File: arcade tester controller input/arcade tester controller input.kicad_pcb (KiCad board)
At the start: 2 copper layers, 70.2 x 88 mm, 27 parts, among them J1 FTDI, J2 ICSP, J3 DE9M 1, J4 DE9M 2, J5 Conn_01x08, J6 Conn_01x08, J7 Conn_01x08, J8 Conn_01x08, J9 Conn_01x02, U1 ATmega328P-P, U2 MCP23018, U3 MCP23018, Y1 16M

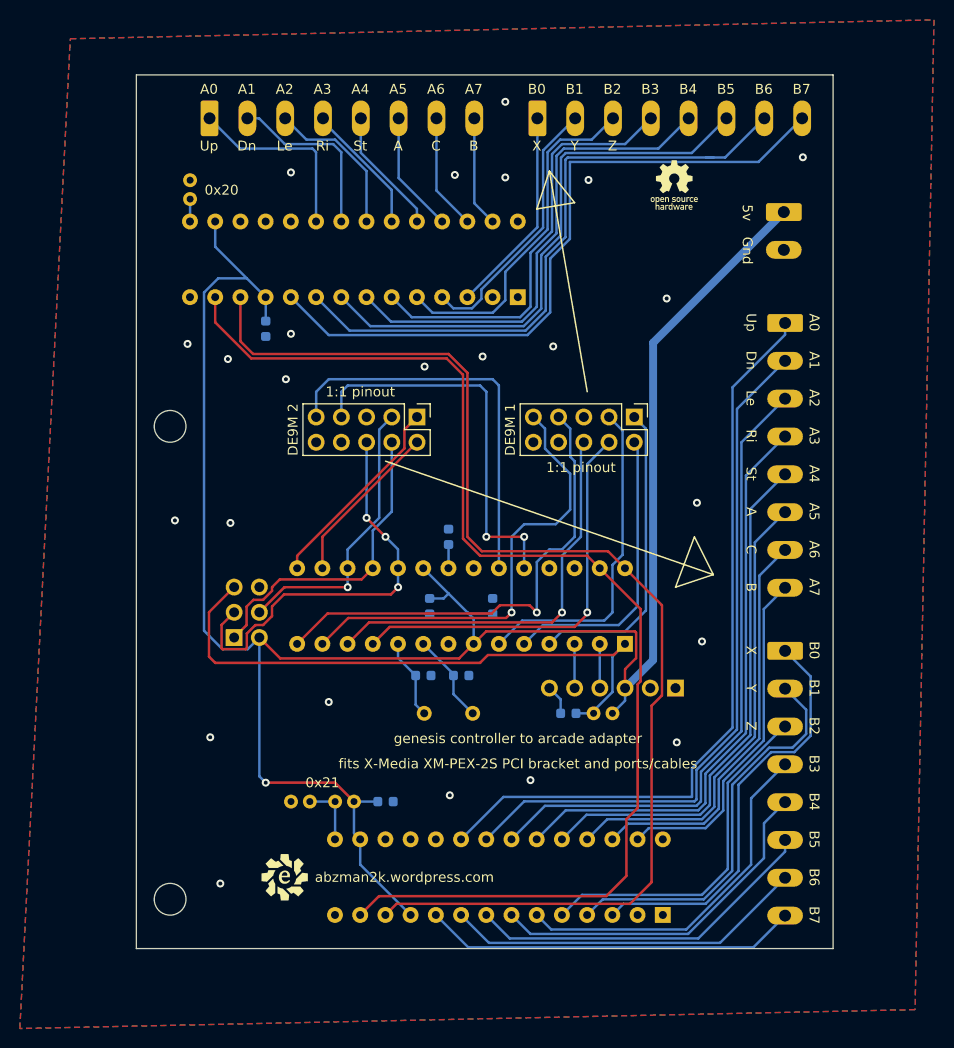
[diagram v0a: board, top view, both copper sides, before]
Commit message: made pcb for pci bracket board
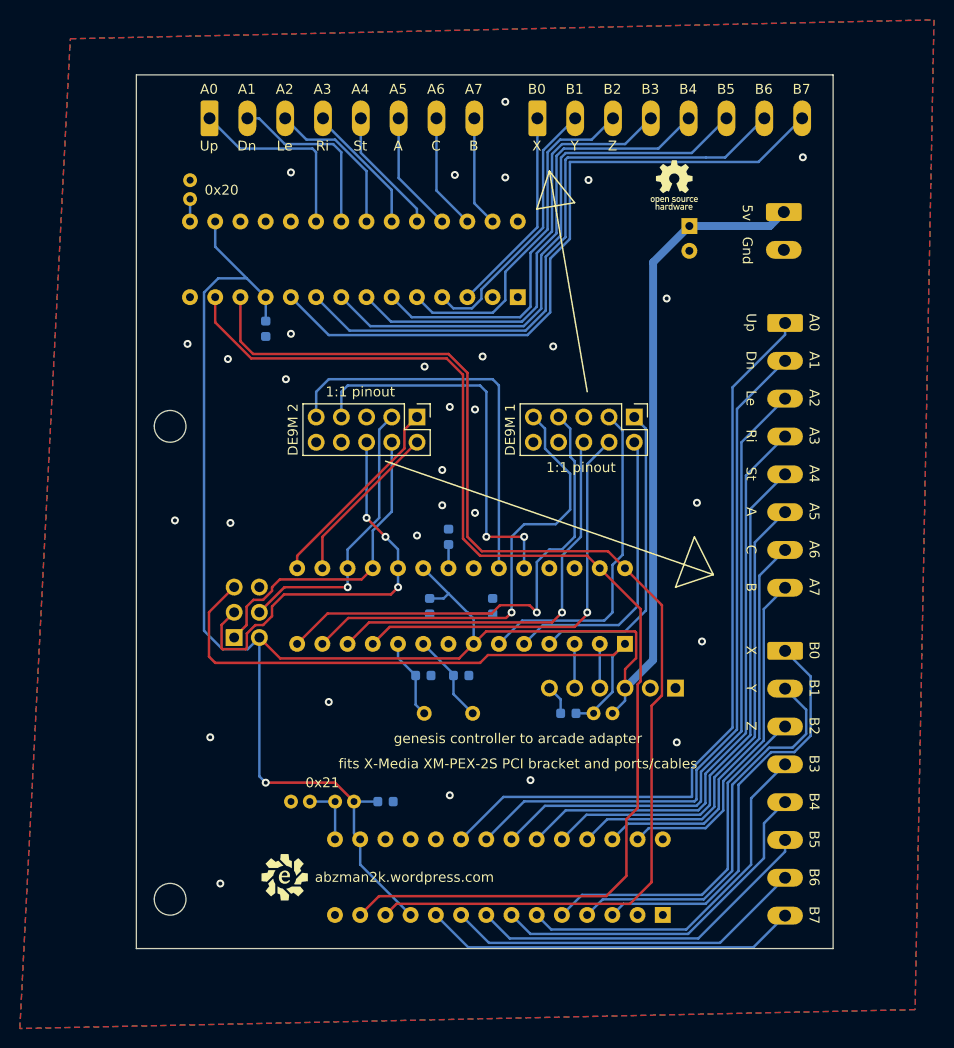
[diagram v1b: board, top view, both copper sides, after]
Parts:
- added C9: 10uF, Capacitor_THT:CP_Radial_D5.0mm_P2.50mm, B.Cu at (172.2, 73.5)
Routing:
- net +5V: track 216.8 -> 221.6 mm
- net Net-(J5-Pad7): track 63.9 -> 63.1 mm
- net GND: vias 24 -> 30

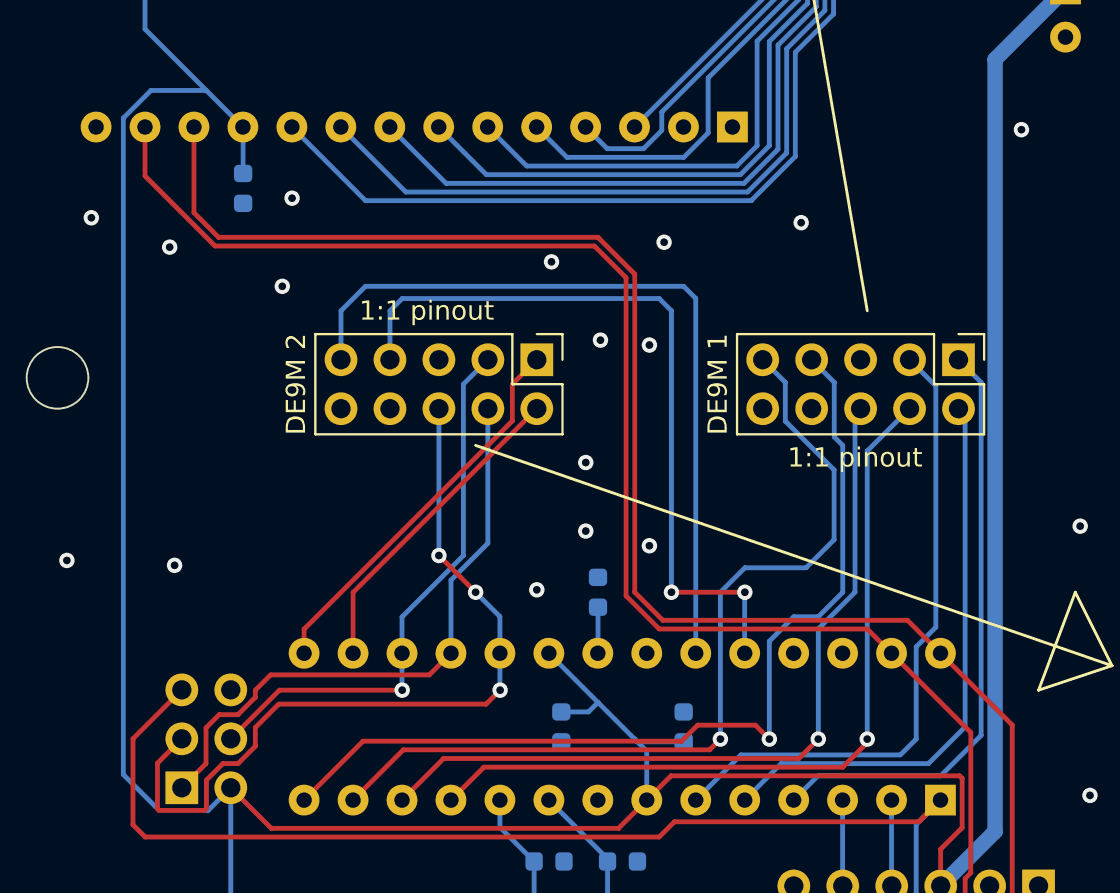
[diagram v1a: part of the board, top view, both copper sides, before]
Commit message: added 5v and gnd to controller ports
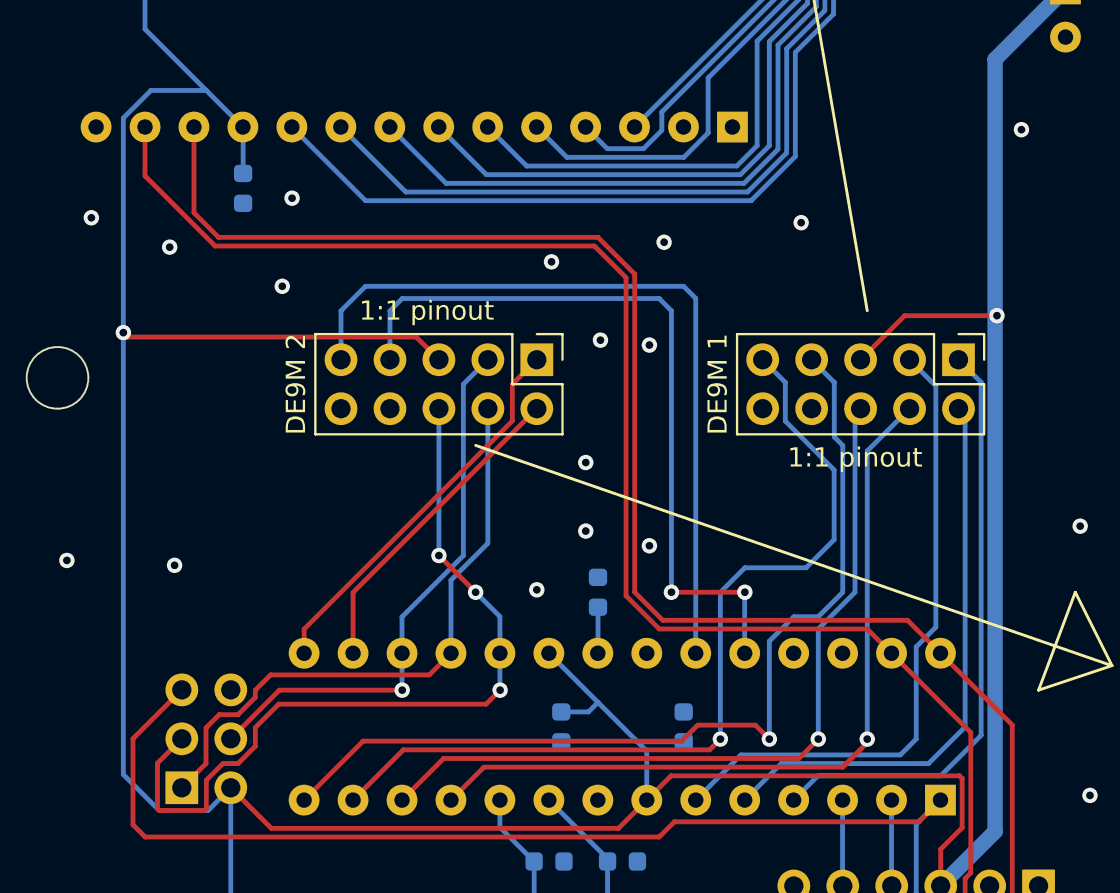
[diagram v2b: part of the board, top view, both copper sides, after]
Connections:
- J3 pad 5: unconnected-(J3-Pad5) -> +5V
- J3 pad 8: unconnected-(J3-Pad8) -> GND
- J4 pad 5: unconnected-(J4-Pad5) -> +5V
- J4 pad 8: unconnected-(J4-Pad8) -> GND
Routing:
- net +5V: track 221.6 -> 246.4 mm, vias 1 -> 3
